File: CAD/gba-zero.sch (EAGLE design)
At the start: 55 parts, among them IC5 APX803, Q2 BSS138, U1 NC7WZ16, U4 LM4875

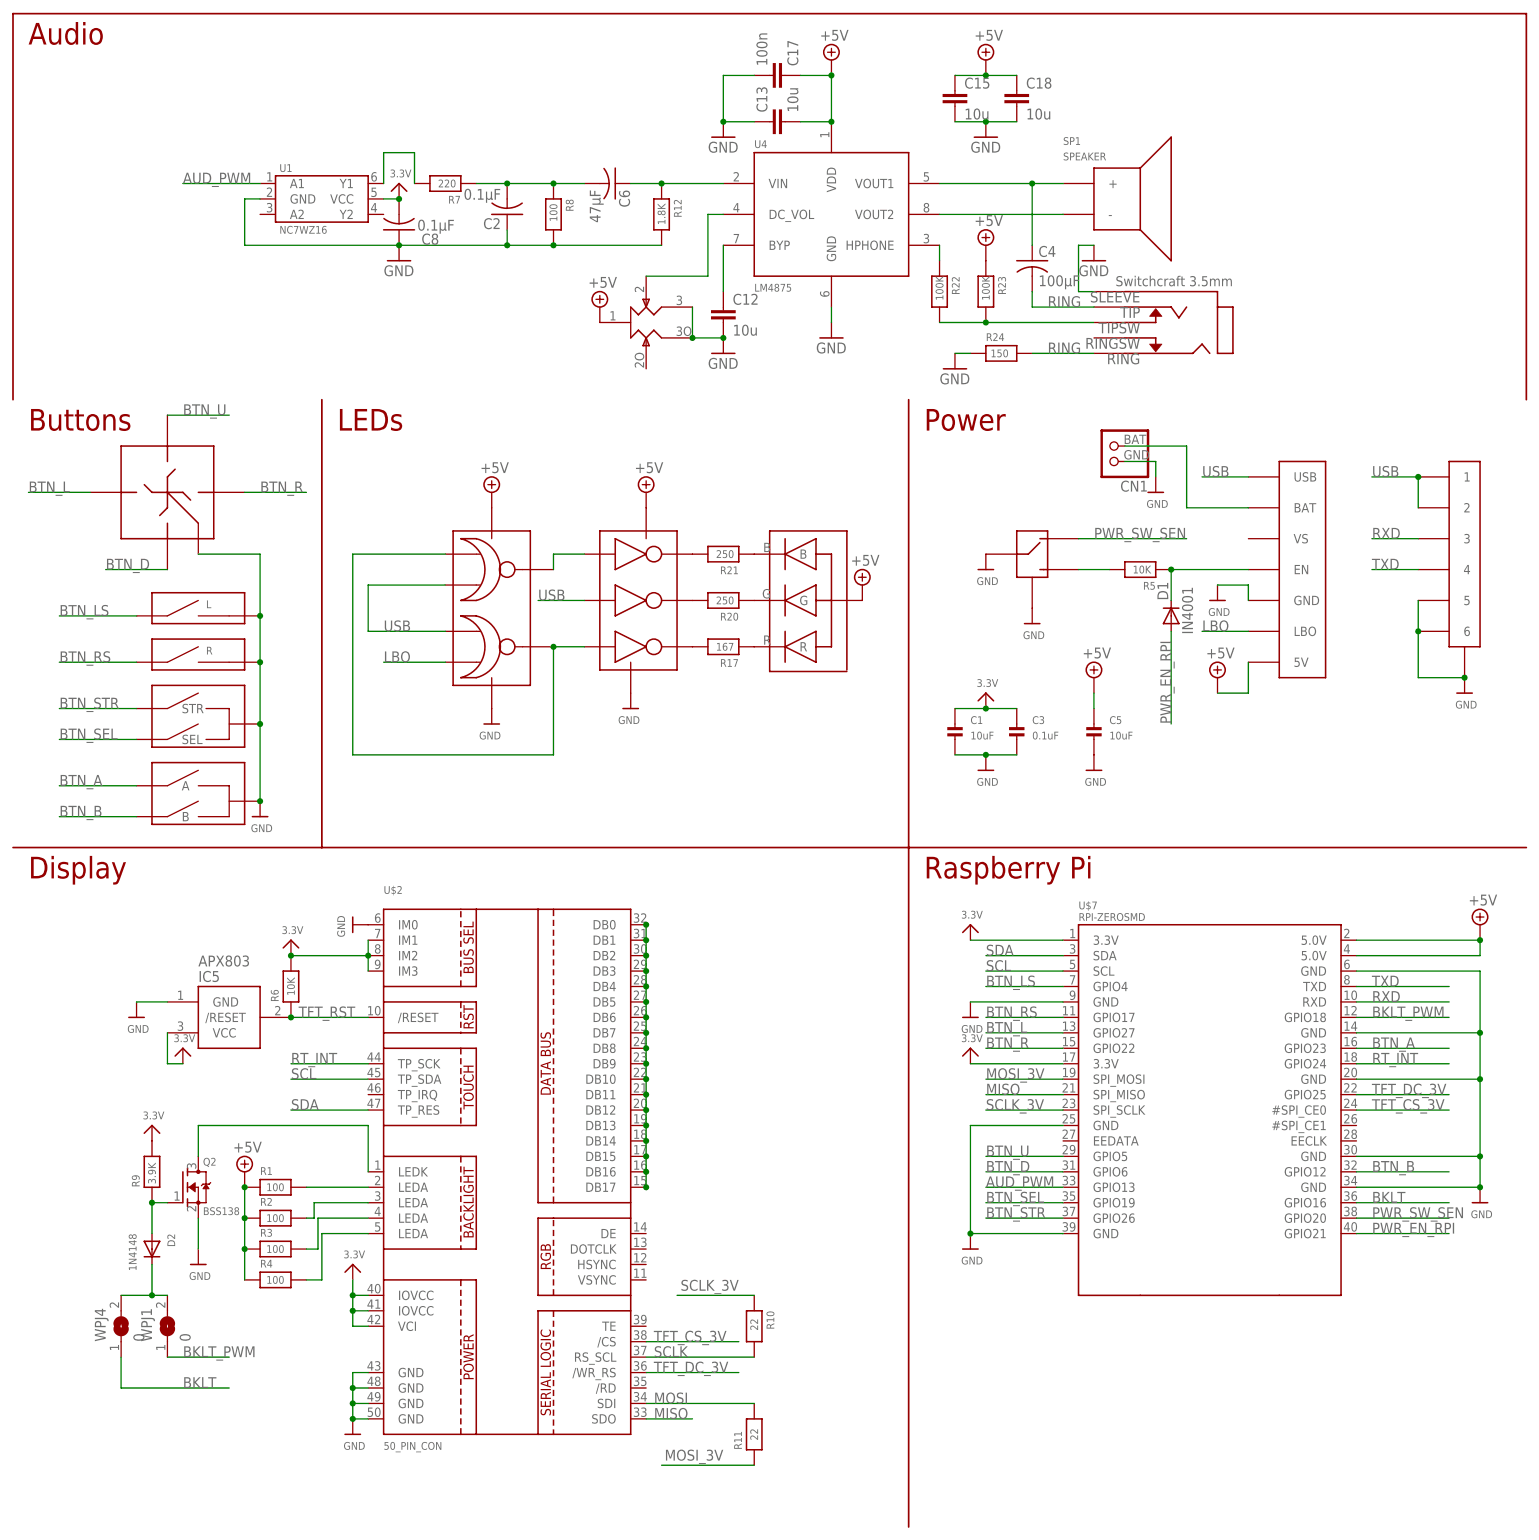
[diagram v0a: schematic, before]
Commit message: Routed right side of the board
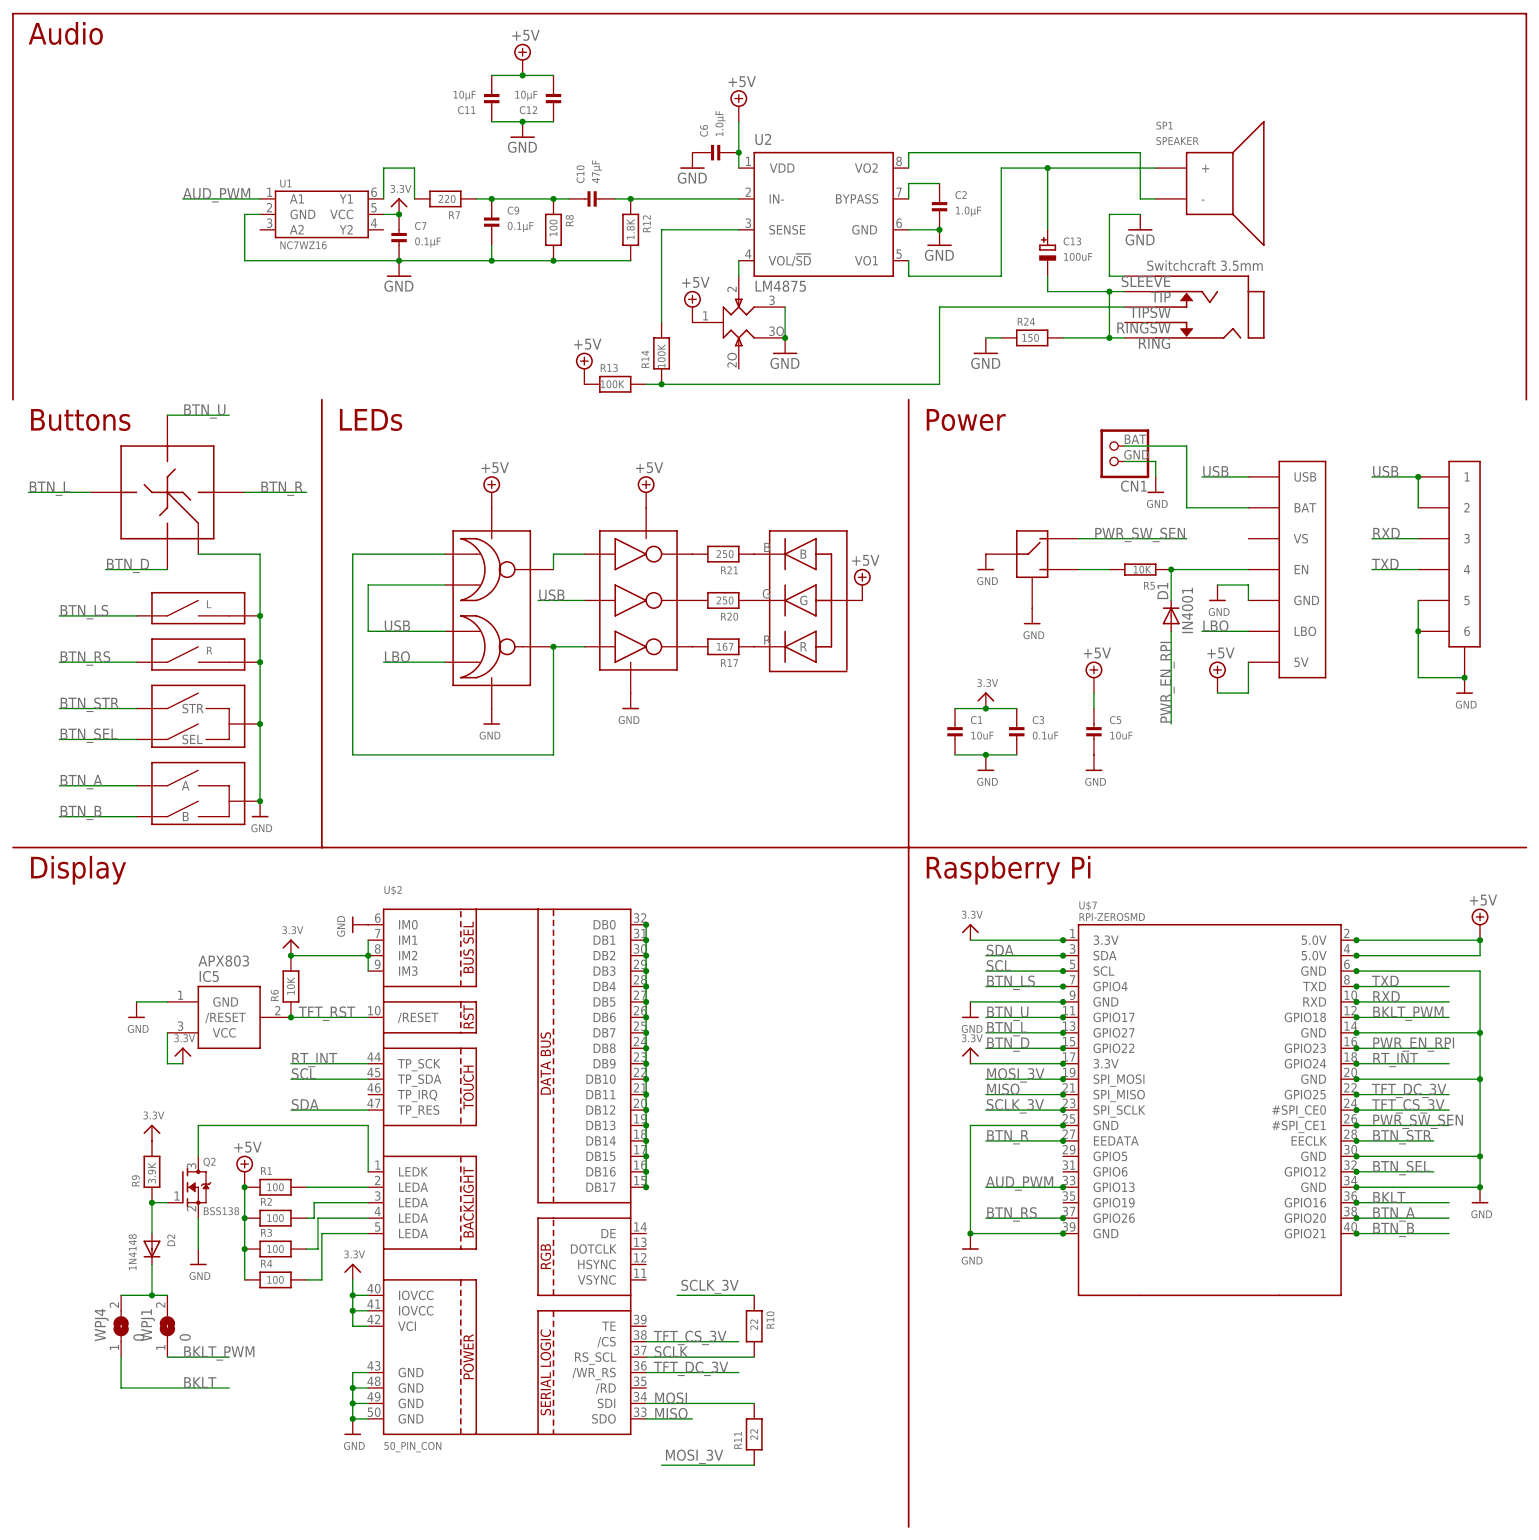
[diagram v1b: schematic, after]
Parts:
- removed C15, C18: 10u, rcl:C-EUC0805
- removed C17: 100n, rcl:C-EUC0805
- removed C4: 100μF, rcl:C-USC0603
- removed C8: 0.1μF, rcl:C-USC0603
- removed R22, R23: 100K, microbuilder:RESISTOR0805
- removed U4: LM4875, texas:LM4875
- added C10: 47μF, microbuilder:CAP_CERAMIC0603
- added C11: 10μF, microbuilder:CAP_CERAMIC0603
- added C7, C9: 0.1μF, microbuilder:CAP_CERAMIC0603
- added R13, R14: 100K, microbuilder:RESISTOR0603
- added U2: LM4875, gba-zero-parts:LM4875
- C12: value 10u -> 10μF; device rcl:C-EUC0805 -> microbuilder:CAP_CERAMIC0603
- C13: value 10u -> 100uF; device rcl:C-EUC0805 -> microbuilder:CAP_ELECTROLYTICPANASONIC_D
- C2: value 0.1μF -> 1.0μF; device rcl:C-USC0603 -> microbuilder:CAP_CERAMIC0603
- C6: value 47μF -> 1.0μF; device rcl:C-USC0603 -> microbuilder:CAP_CERAMIC0603
- D1: device diode:DIODE-D-5 -> diode:DIODE-D-7.5
- R12, R24, R7, R8: device microbuilder:RESISTOR0805 -> microbuilder:RESISTOR0603
- R5: device microbuilder:RESISTOR0805 -> resistor:R-EU_0204/7
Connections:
- net N$19 renamed BAT
- removed net N$23: R22.1, U4.HPHONE
- removed net N$26: U$17.2, U4.DC_VOL
- removed net N$30: C6.1, R12.1, U4.VIN
- removed net N$35: C12.1, U4.BYP
- removed net N$36: C4.1, SP1.+, U4.VOUT1
- removed net N$37: SP1.-, U4.VOUT2
- new net BYPASS: C2.P$1, U2.BYPASS
- new net IN-: C10.P$2, R12.1, U2.IN-
- new net SENSE: R14.2, U2.SENSE
- new net VO1: C13.+, SP1.+, U2.VO1
- new net VO2: SP1.-, U2.VO2
- new net VOL/SD: U$17.2, U2.VOL/!SD
- net +5V: now also C11.P$2, C12.P$2, C6.P$2, R13.1, U2.VDD; no longer C13.2, C15.1, C17.1, C18.1, R23.1, U4.VDD
- net 3.3V: now also C7.P$1; no longer C8.2
- net BTN_A: now also U$7.GPIO20; no longer U$7.GPIO23
- net BTN_B: now also U$7.GPIO21; no longer U$7.GPIO12
- net BTN_D: now also U$7.GPIO22; no longer U$7.GPIO6
- net BTN_R: now also U$7.EEDATA; no longer U$7.GPIO22
- net BTN_RS: now also U$7.GPIO26; no longer U$7.GPIO17
- net BTN_SEL: now also U$7.GPIO12; no longer U$7.GPIO19
- net BTN_STR: now also U$7.EECLK; no longer U$7.GPIO26
- net BTN_U: now also U$7.GPIO17; no longer U$7.GPIO5
- net GND: now also C11.P$1, C12.P$1, C2.P$2, C6.P$1, C7.P$2, C9.P$2, U2.GND@; no longer C12.2, C13.1, C15.2, C17.2, C18.2, C2.1, C8.1, U4.GND
- net N$21: now also C10.P$1, C9.P$1; no longer C2.2, C6.2
- net N$22: now also R13.2, R14.1; no longer R22.2, R23.2
- net PWR_EN_RPI: now also U$7.GPIO23; no longer U$7.GPIO21
- net PWR_SW_SEN: now also U$7.#SPI_CE1; no longer U$7.GPIO20
- net RING: now also C13.-; no longer C4.2
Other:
- moved on the sheet: C12, C2, C6, R12, R24, R7, R8, SP1, U1

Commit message: More Routing
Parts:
- added C14, C4: 10μF, microbuilder:CAP_CERAMIC0603
- added C8: 0.1μF, microbuilder:CAP_CERAMIC0603
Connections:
- net +5V: now also C14.P$1
- net 3.3V: now also C4.P$1, C8.P$1
- net GND: now also C14.P$2, C4.P$2, C8.P$2
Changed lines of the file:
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@@
 <part name="SUPPLY8" library="supply2" deviceset="+5V" device=""/>
 <part name="R14" library="microbuilder" deviceset="RESISTOR" device="0603" value="100K"/>
+<part name="C4" library="microbuilder" deviceset="CAP_CERAMIC" device="0603" value="10μF"/>
+<part name="C8" library="microbuilder" deviceset="CAP_CERAMIC" device="0603" value="0.1μF"/>
+<part name="C14" library="microbuilder" deviceset="CAP_CERAMIC" device="0603" value="10μF"/>
+<part name="U$24" library="microbuilder" deviceset="3.3V" device=""/>
+<part name="U$28" library="microbuilder" deviceset="GND" device=""/>
+<part name="U$30" library="microbuilder" deviceset="GND" device=""/>
+<part name="SUPPLY11" library="supply2" deviceset="+5V" device=""/>
 </parts>
 <sheets>
@@
 <attribute name="VALUE" x="107.315" y="190.5" size="1.27" layer="96" font="vector" rot="R90"/>
 </instance>
+<instance part="C4" gate="G$1" x="111.76" y="83.82"/>
+<instance part="C8" gate="G$1" x="124.46" y="83.82"/>
+<instance part="C14" gate="G$1" x="137.16" y="83.82"/>
+<instance part="U$24" gate="G$1" x="119.38" y="91.44"/>
+<instance part="U$28" gate="G$1" x="137.16" y="78.74"/>
+<instance part="U$30" gate="G$1" x="119.38" y="78.74"/>
+<instance part="SUPPLY11" gate="+5V" x="137.16" y="91.44"/>
 </instances>
 <busses>
@@
 <pinref part="C6" gate="G$1" pin="P$1"/>
 <pinref part="GND9" gate="1" pin="GND"/>
+</segment>
+<segment>
+<pinref part="C14" gate="G$1" pin="P$2"/>
+<pinref part="U$28" gate="G$1" pin="GND"/>
+</segment>
+<segment>
+<pinref part="C4" gate="G$1" pin="P$2"/>
+<pinref part="C8" gate="G$1" pin="P$2"/>
+<wire x1="111.76" y1="81.28" x2="119.38" y2="81.28" width="0.1524" layer="91"/>
+<pinref part="U$30" gate="G$1" pin="GND"/>
+<wire x1="119.38" y1="81.28" x2="124.46" y2="81.28" width="0.1524" layer="91"/>
+<junction x="119.38" y="81.28"/>
 </segment>
 </net>
@@
 <junction x="160.02" y="134.62"/>
 </segment>
+<segment>
+<pinref part="C4" gate="G$1" pin="P$1"/>
+<pinref part="C8" gate="G$1" pin="P$1"/>
+<wire x1="111.76" y1="88.9" x2="119.38" y2="88.9" width="0.1524" layer="91"/>
+<pinref part="U$24" gate="G$1" pin="3.3V"/>
+<wire x1="119.38" y1="88.9" x2="124.46" y2="88.9" width="0.1524" layer="91"/>
+<junction x="119.38" y="88.9"/>
+</segment>
 </net>
 <net name="N$6" class="0">
@@
 <junction x="119.38" y="226.06"/>
 </segment>
-</net>
+<segment>
+<pinref part="C14" gate="G$1" pin="P$1"/>
+<pinref part="SUPPLY11" gate="+5V" pin="+5V"/>
+</segment>
+</net>

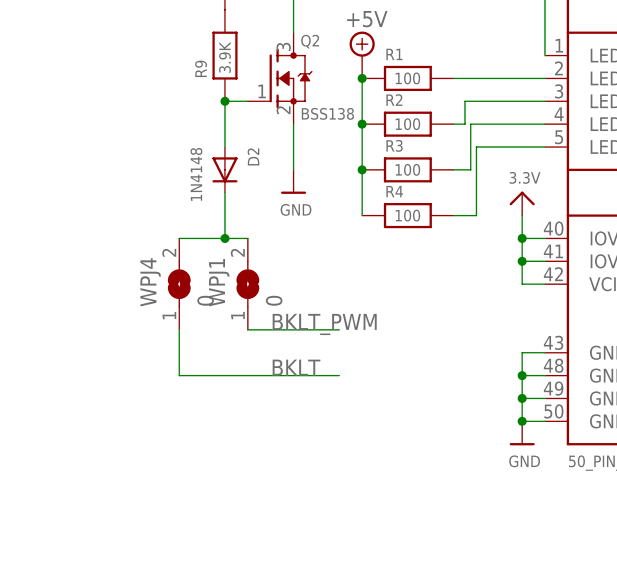
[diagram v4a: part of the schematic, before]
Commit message: Cleared all DRC errors
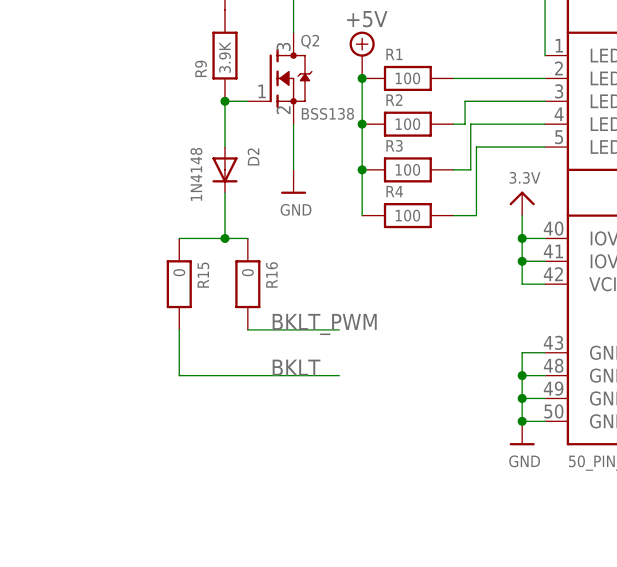
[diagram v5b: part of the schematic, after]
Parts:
- removed WPJ1, WPJ4: 0, microbuilder:SOLDERJUMPERCLOSED
- added R15, R16: 0, microbuilder:RESISTOR0603
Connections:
- net BKLT: now also R15.2; no longer WPJ4.1
- net BKLT_PWM: now also R16.2; no longer WPJ1.1
- net N$6: now also R15.1, R16.1; no longer WPJ1.2, WPJ4.2
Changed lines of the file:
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@@
 <part name="U$34" library="microbuilder" deviceset="3.3V" device=""/>
 <part name="U$41" library="microbuilder" deviceset="GND" device=""/>
-<part name="WPJ1" library="microbuilder" deviceset="SOLDERJUMPER" device="CLOSED" value="0"/>
 <part name="D2" library="microbuilder" deviceset="DIODE" device="SOD-323" value="1N4148"/>
 <part name="Q2" library="microbuilder" deviceset="MOSFET-N" device="WIDE" value="BSS138"/>
@@
 <part name="U$15" library="microbuilder" deviceset="3.3V" device=""/>
 <part name="GND2" library="SparkFun-Aesthetics" deviceset="GND" device=""/>
-<part name="WPJ4" library="microbuilder" deviceset="SOLDERJUMPER" device="CLOSED" value="0"/>
 <part name="R17" library="microbuilder" deviceset="RESISTOR" device="0805" value="167"/>
 <part name="R20" library="microbuilder" deviceset="RESISTOR" device="0805" value="250"/>
@@
 <part name="U$30" library="microbuilder" deviceset="GND" device=""/>
 <part name="SUPPLY11" library="supply2" deviceset="+5V" device=""/>
+<part name="R15" library="microbuilder" deviceset="RESISTOR" device="0603" value="0"/>
+<part name="R16" library="microbuilder" deviceset="RESISTOR" device="0603" value="0"/>
 </parts>
 <sheets>
@@
 <instance part="U$34" gate="G$1" x="55.88" y="43.18"/>
 <instance part="U$41" gate="G$1" x="157.48" y="45.72"/>
-<instance part="WPJ1" gate="1" x="25.4" y="33.02" rot="R90"/>
 <instance part="D2" gate="G$1" x="22.86" y="45.72" rot="R270"/>
 <instance part="Q2" gate="G$1" x="27.94" y="55.88" smashed="yes">
@@
 <instance part="U$15" gate="G$1" x="63.5" y="218.44"/>
 <instance part="GND2" gate="1" x="63.5" y="205.74"/>
-<instance part="WPJ4" gate="1" x="17.78" y="33.02" rot="R90"/>
 <instance part="R17" gate="G$1" x="116.84" y="144.78" smashed="yes" rot="R180">
 <attribute name="NAME" x="119.38" y="142.748" size="1.27" layer="95" font="vector" rot="R180"/>
@@
 <instance part="U$30" gate="G$1" x="119.38" y="78.74"/>
 <instance part="SUPPLY11" gate="+5V" x="137.16" y="91.44"/>
+<instance part="R15" gate="G$1" x="17.78" y="33.02" smashed="yes" rot="R270">
+<attribute name="NAME" x="19.812" y="35.56" size="1.27" layer="95" font="vector" rot="R270"/>
+<attribute name="VALUE" x="17.145" y="34.798" size="1.27" layer="96" font="vector" rot="R270"/>
+</instance>
+<instance part="R16" gate="G$1" x="25.4" y="33.02" smashed="yes" rot="R270">
+<attribute name="NAME" x="27.432" y="35.56" size="1.27" layer="95" font="vector" rot="R270"/>
+<attribute name="VALUE" x="24.765" y="34.798" size="1.27" layer="96" font="vector" rot="R270"/>
+</instance>
 </instances>
 <busses>
@@
 <wire x1="35.56" y1="27.94" x2="25.4" y2="27.94" width="0.1524" layer="91"/>
 <label x="27.94" y="27.94" size="1.778" layer="95"/>
-<pinref part="WPJ1" gate="1" pin="1"/>
+<pinref part="R16" gate="G$1" pin="2"/>
 </segment>
 <segment>
@@
 <net name="N$6" class="0">
 <segment>
-<pinref part="WPJ1" gate="1" pin="2"/>
 <pinref part="D2" gate="G$1" pin="C"/>
-<pinref part="WPJ4" gate="1" pin="2"/>
 <wire x1="25.4" y1="38.1" x2="22.86" y2="38.1" width="0.1524" layer="91"/>
 <wire x1="22.86" y1="38.1" x2="17.78" y2="38.1" width="0.1524" layer="91"/>
 <wire x1="22.86" y1="43.18" x2="22.86" y2="38.1" width="0.1524" layer="91"/>
 <junction x="22.86" y="38.1"/>
+<pinref part="R16" gate="G$1" pin="1"/>
+<pinref part="R15" gate="G$1" pin="1"/>
 </segment>
 </net>
@@
 <wire x1="17.78" y1="22.86" x2="35.56" y2="22.86" width="0.1524" layer="91"/>
 <label x="27.94" y="22.86" size="1.778" layer="95"/>
-<pinref part="WPJ4" gate="1" pin="1"/>
 <wire x1="17.78" y1="27.94" x2="17.78" y2="22.86" width="0.1524" layer="91"/>
-</segment>
-</net>
+<pinref part="R15" gate="G$1" pin="2"/>
+</segment>
+</net>
